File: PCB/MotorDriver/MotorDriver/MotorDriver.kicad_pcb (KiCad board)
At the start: 2 copper layers, 101.3 x 73.7 mm, 92 parts, among them J1 XT30PW-M, J10 JST-XH, J11 JST-XH, J12 JST-XH, J13 JST-XH, J14 JST-XH, J15 JST-XH, J16 JST-XH, J17 JST-XH, J18 JST-XH, J19 JST-XH, J2 JST-XH, J20 JST-XH, J21 JST-XH, J22 JST-XH, J23 JST-XH, J24 JST-XH, J3 XT30PW-M, J4 XT30PW-M, J5 JST-XH, J6 JST-XH, J7 JST-XH, J8 JST-XH, J9 JST-XH, Q1 TJ60S04M3L, Q10 NMOS, Q2 NMOS, Q3 NMOS, Q4 NMOS, Q5 NMOS, Q6 NMOS, Q7 NMOS, Q8 NMOS, Q9 NMOS, SW1 SW_DPST_x2, SW2 SW_Push, SW3 SW_Push, U1 DRV8701ERGET, U2 DRV8701ERGET, U3 TCA9548APWR, U4 Pico, U5 AZ1117CH-3.3TR

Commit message: :sparkles: Production Done
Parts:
- moved Q2 0.29 mm to (132.6, 148.2), turned to 180 degrees
- moved Q4 0.28 mm to (132.6, 167.1), turned to 180 degrees
- moved Q3 0.27 mm to (132.7, 154.4), turned to 0 degrees
- moved Q9 0.27 mm to (132.7, 160.8), turned to 0 degrees
- moved Q7 0.17 mm to (132.7, 119.9), turned to 180 degrees
- moved Q5 0.17 mm to (132.7, 138.9), turned to 180 degrees
- moved Q6 0.16 mm to (132.7, 132.6), turned to 0 degrees
- moved Q8 0.16 mm to (132.7, 126.2), turned to 0 degrees
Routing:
- net Net-(Q2-G): track 4.60 -> 14.9 mm
- net Net-(Q7-G): track 4.60 -> 14.3 mm
- net Motor2A: track 17.6 -> 21.0 mm
- net Motor1A: track 17.6 -> 20.9 mm
- net Motor1B: track 15.0 -> 12.7 mm
- net Motor2B: track 15.0 -> 13.0 mm
- net Net-(Q9-G): track 14.2 -> 12.4 mm
- net Net-(Q6-G): track 14.2 -> 12.4 mm
- net Net-(Q5-G): track 20.6 -> 19.9 mm
- net Net-(Q3-G): track 11.3 -> 10.7 mm
- net GND: vias 180 -> 155
- net +12V: vias 48 -> 43

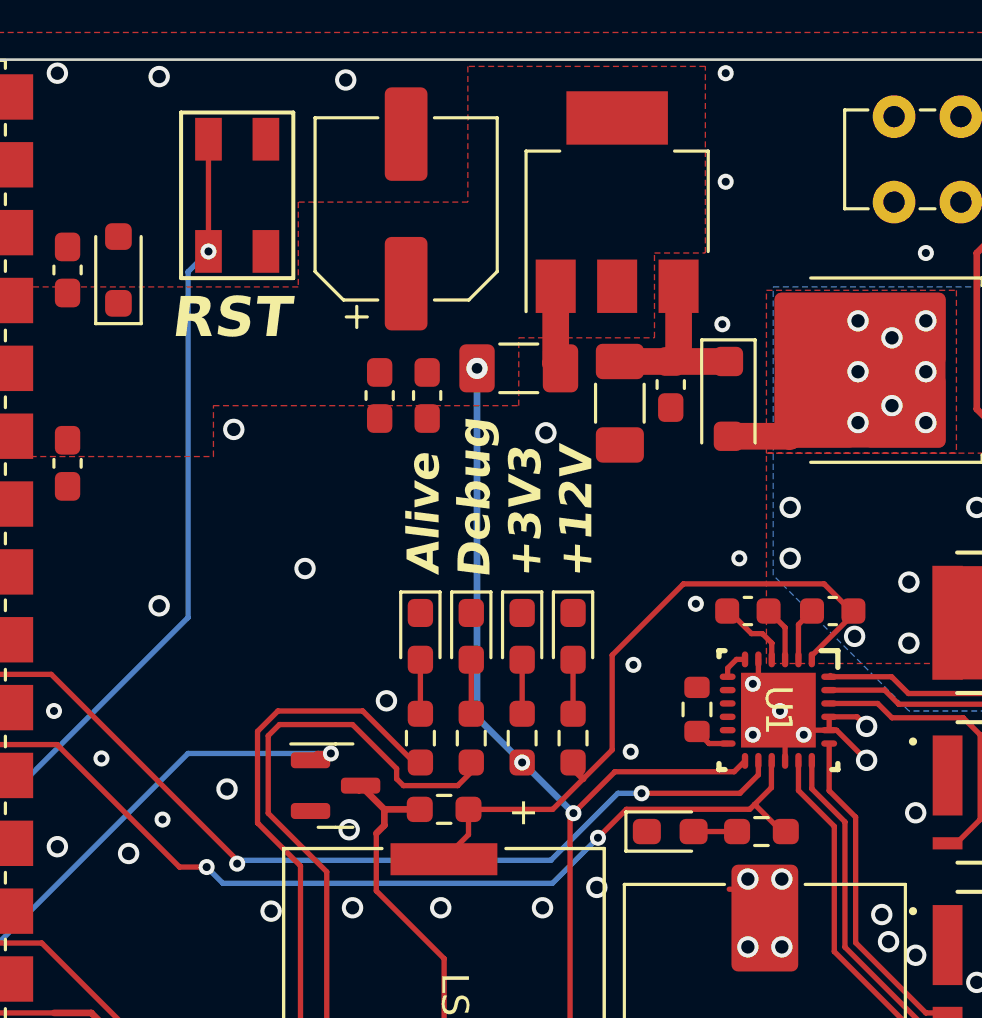
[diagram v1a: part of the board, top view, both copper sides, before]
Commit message: ✏️ [PCB] モータからの逆起電力対策ダイオードを追加
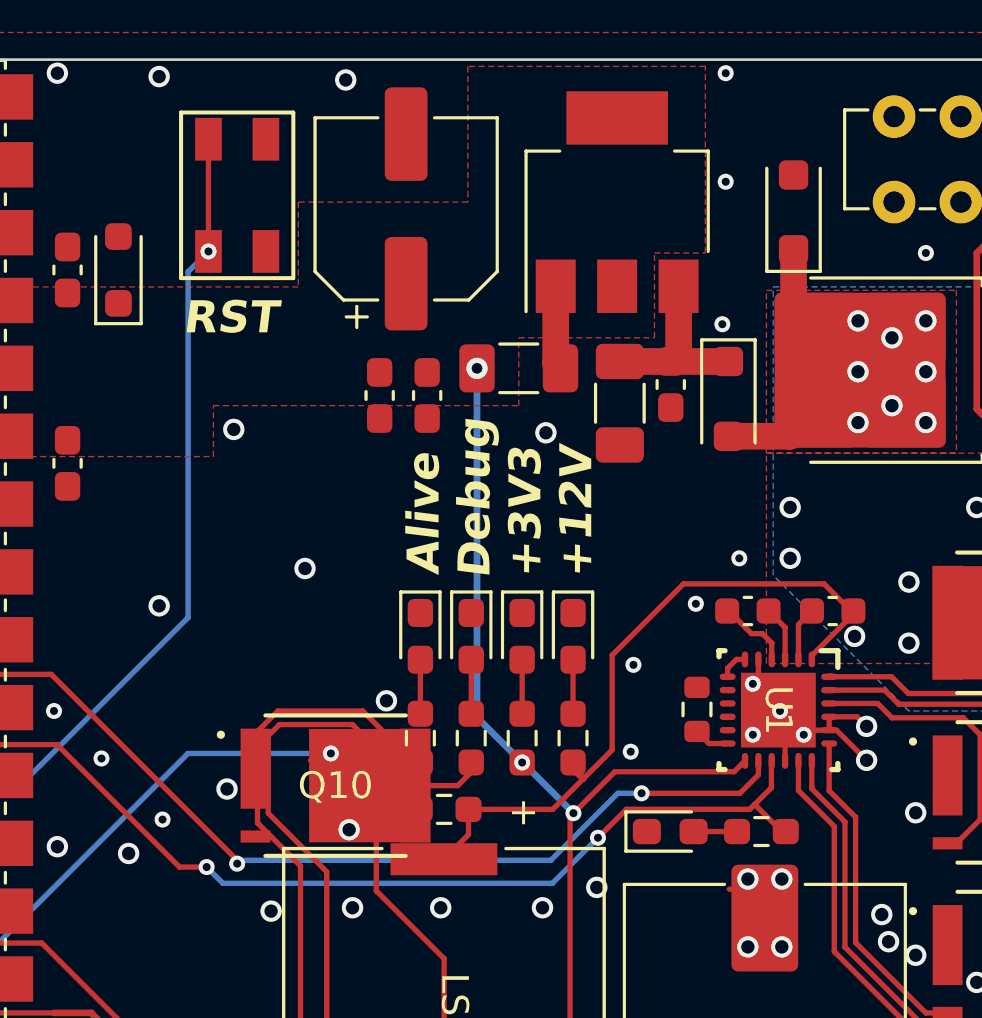
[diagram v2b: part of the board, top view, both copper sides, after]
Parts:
- added D2: ＧＳ１０１０ＦＬ, Diode_SMD:D_SOD-123F, F.Cu at (124.0, 104.5)
- Q10: footprint Package_TO_SOT_SMD:SOT-23 -> TPH11006NL:TPH11006NL_SOP Advance_TOS-M
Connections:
- R2 pad 2: Net-(Q1-G) -> GND
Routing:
- net GND: track 32.4 -> 44.7 mm
- net Net-(Q1-G): track 12.3 -> 0.00 mm
- net +12V: track 65.1 -> 68.8 mm

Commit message: ✏️ 昔のファイルを引っ張てきた
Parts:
- removed D2: ＧＳ１０１０ＦＬ, Diode_SMD:D_SOD-123F
- Q10: footprint TPH11006NL:TPH11006NL_SOP Advance_TOS-M -> Package_TO_SOT_SMD:SOT-23
- moved Q2 0.29 mm to (132.9, 148.1), turned to 0 degrees
- moved Q4 0.28 mm to (132.9, 167.1), turned to 0 degrees
- moved Q3 0.27 mm to (132.9, 154.4), turned to 180 degrees
- moved Q9 0.27 mm to (132.9, 160.8), turned to 180 degrees
- moved Q7 0.17 mm to (132.9, 120.0), turned to 0 degrees
- moved Q5 0.17 mm to (132.9, 139.0), turned to 0 degrees
- moved Q6 0.16 mm to (132.9, 132.7), turned to 180 degrees
- moved Q8 0.16 mm to (132.9, 126.3), turned to 180 degrees
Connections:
- R2 pad 2: GND -> Net-(Q1-G)
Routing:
- net GND: track 44.7 -> 32.4 mm, vias 155 -> 180
- net Net-(Q1-G): track 0.00 -> 12.3 mm
- net Net-(Q2-G): track 14.9 -> 4.60 mm
- net Net-(Q7-G): track 14.3 -> 4.60 mm
- net +12V: track 68.8 -> 65.1 mm, vias 43 -> 48
- net Motor2A: track 21.0 -> 17.6 mm
- net Motor1A: track 20.9 -> 17.6 mm
- net Motor1B: track 12.7 -> 15.0 mm
- net Motor2B: track 13.0 -> 15.0 mm
- net Net-(Q9-G): track 12.4 -> 14.2 mm
- net Net-(Q6-G): track 12.4 -> 14.2 mm
- net Net-(Q5-G): track 19.9 -> 20.6 mm
- net Net-(Q3-G): track 10.7 -> 11.3 mm
